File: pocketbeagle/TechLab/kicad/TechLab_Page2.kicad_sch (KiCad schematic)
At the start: 50 parts, among them J2 USB_C_Receptacle_USB2.0, J5 JST-SH-3P, T1 EAALSTIC1708A0, T2 3904, U5 MCP23S18-E/MJ, U6 FT230XQ-R, U7 SN74LV4053A

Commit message: TechLab: fix some reference designators
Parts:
- renumbered C11 to C10, C8 to C11, C9 to C8, R3 to R1, R7 to R10, R23 to R19, R4 to R2, R24 to R20, R10 to R21, R21 to R22, R6 to R3, R22 to R4, R9 to R6, R2 to R7, R1 to R9, T2 to T1, T1 to T2
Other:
- moved on the sheet: J5, R25, U7

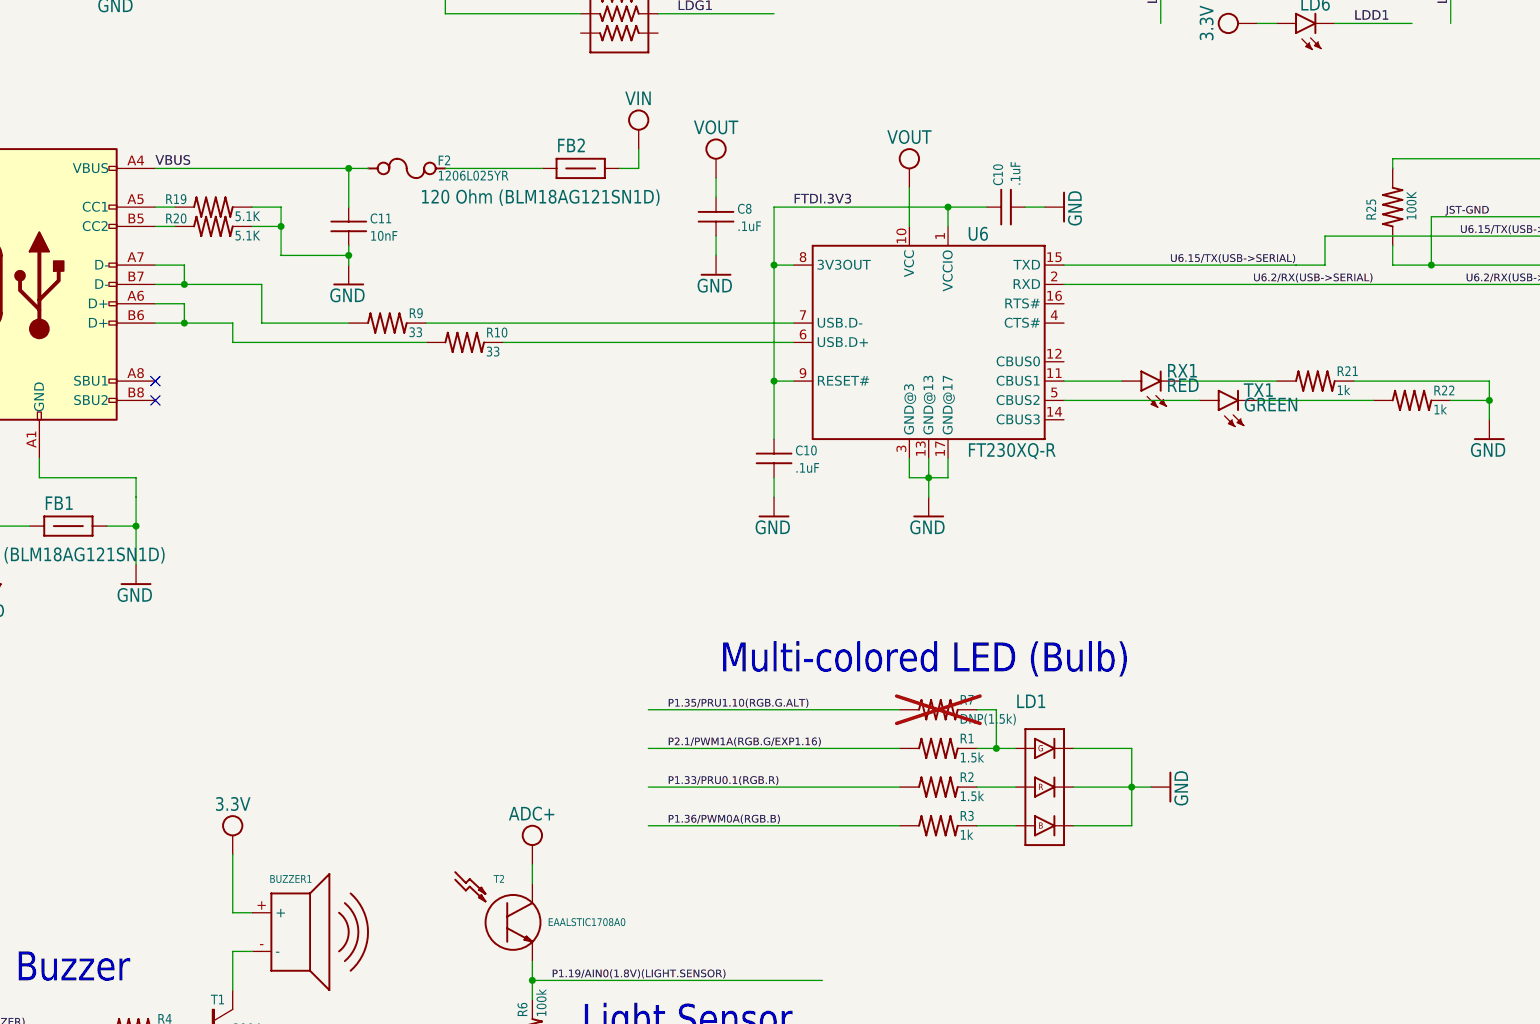
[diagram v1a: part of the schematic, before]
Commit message: TechLab: BOM and RefDes updates
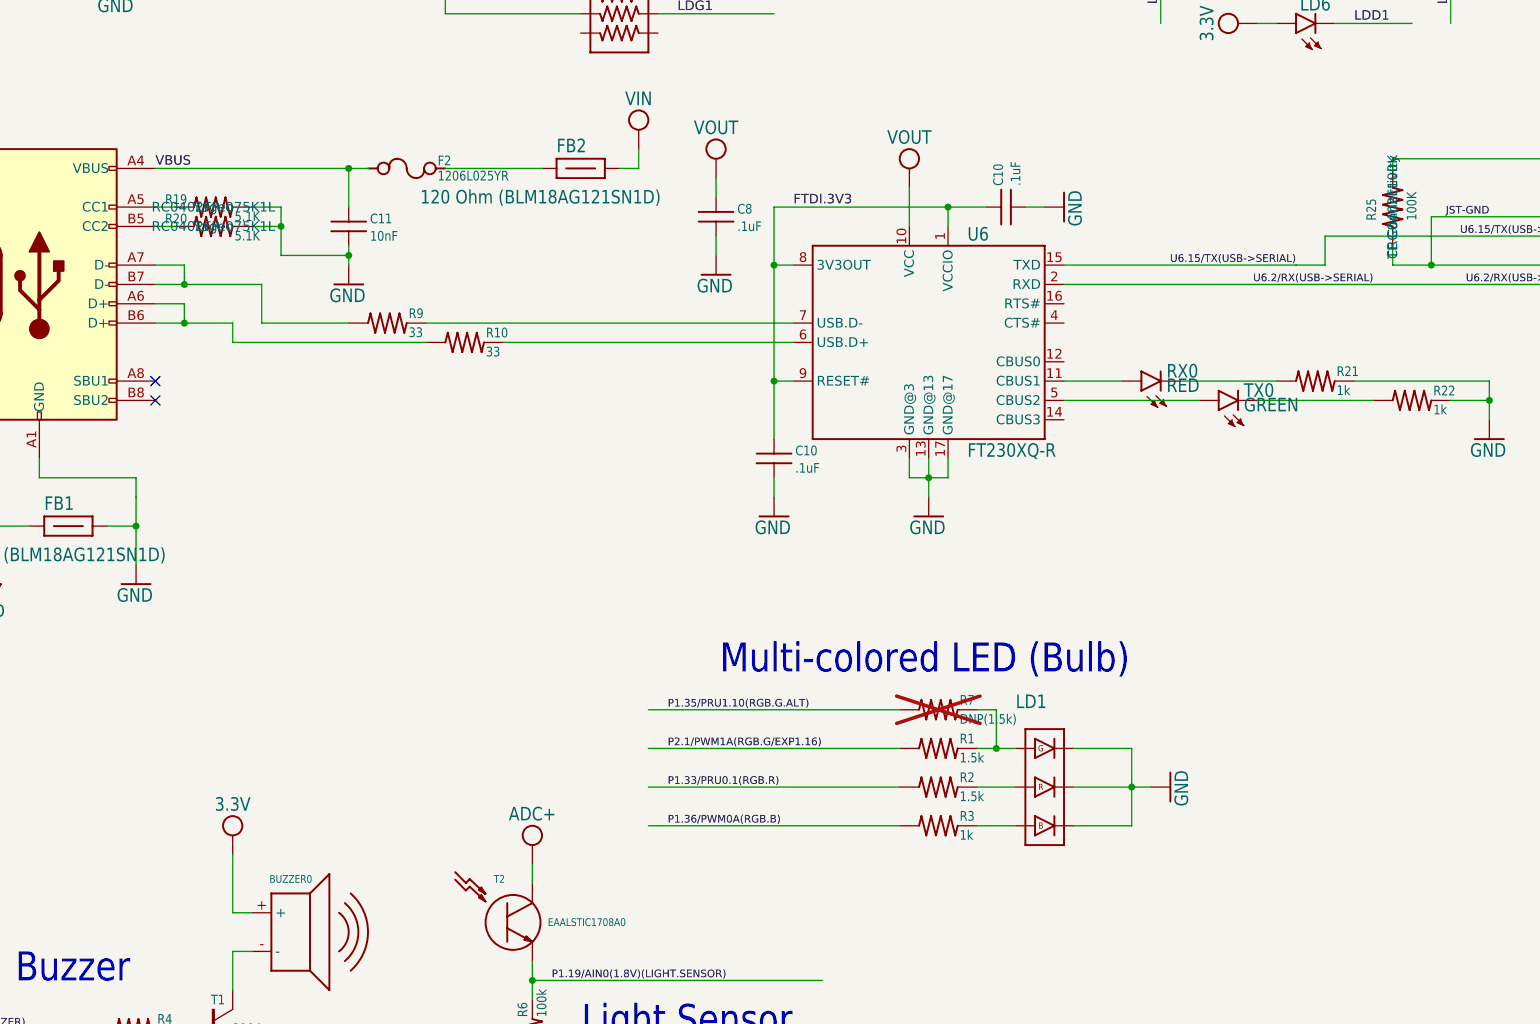
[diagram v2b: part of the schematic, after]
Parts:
- R19, R20: MANUFACTURER (none) -> Yageo; MPN (none) -> RC0402FR-075K1L
- R25: MANUFACTURER (none) -> TE Connectivity; MPN (none) -> CRG0402F100K
- renumbered BUZZER1 to BUZZER0, RX1 to RX0, TX1 to TX0
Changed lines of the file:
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@@
 		(on_board yes)
 		(dnp no)
-		(property "Reference" "RX1"
+		(property "Reference" "RX0"
 			(at 172.212 114.046 90)
 			(effects
@@
 			(project "TechLab"
 				(path "/199e843b-8c9a-4ca8-a6e6-fde18a374d00/4dffbcbf-91b6-4a9c-9fc6-f872a45552ad"
-					(reference "RX1")
+					(reference "RX0")
 					(unit 1)
 				)
@@
 			)
 		)
-		(property "MPN" ""
+		(property "MPN" "RC0402FR-075K1L"
+			(at 46.99 93.98 0)
+			(effects
+				(font
+					(size 1.27 1.27)
+				)
+			)
+		)
+		(property "MANUFACTURER" "Yageo"
 			(at 46.99 93.98 0)
 			(effects
@@
 		(on_board yes)
 		(dnp no)
-		(property "Reference" "BUZZER1"
+		(property "Reference" "BUZZER0"
 			(at 54.356 180.34 0)
 			(effects
@@
 			(project "TechLab"
 				(path "/199e843b-8c9a-4ca8-a6e6-fde18a374d00/4dffbcbf-91b6-4a9c-9fc6-f872a45552ad"
-					(reference "BUZZER1")
+					(reference "BUZZER0")
 					(unit 1)
 				)
@@
 			)
 		)
-		(property "MPN" ""
+		(property "MPN" "CRG0402F100K"
+			(at 201.93 91.44 0)
+			(effects
+				(font
+					(size 1.27 1.27)
+				)
+			)
+		)
+		(property "MANUFACTURER" "TE Connectivity"
 			(at 201.93 91.44 0)
 			(effects
@@
 		(on_board yes)
 		(dnp no)
-		(property "Reference" "TX1"
+		(property "Reference" "TX0"
 			(at 182.372 116.586 90)
 			(effects
@@
 			(project "TechLab"
 				(path "/199e843b-8c9a-4ca8-a6e6-fde18a374d00/4dffbcbf-91b6-4a9c-9fc6-f872a45552ad"
-					(reference "TX1")
+					(reference "TX0")
 					(unit 1)
 				)
@@
 			)
 		)
-		(property "MPN" ""
+		(property "MPN" "RC0402FR-075K1L"
+			(at 46.99 91.44 0)
+			(effects
+				(font
+					(size 1.27 1.27)
+				)
+			)
+		)
+		(property "MANUFACTURER" "Yageo"
 			(at 46.99 91.44 0)
 			(effects

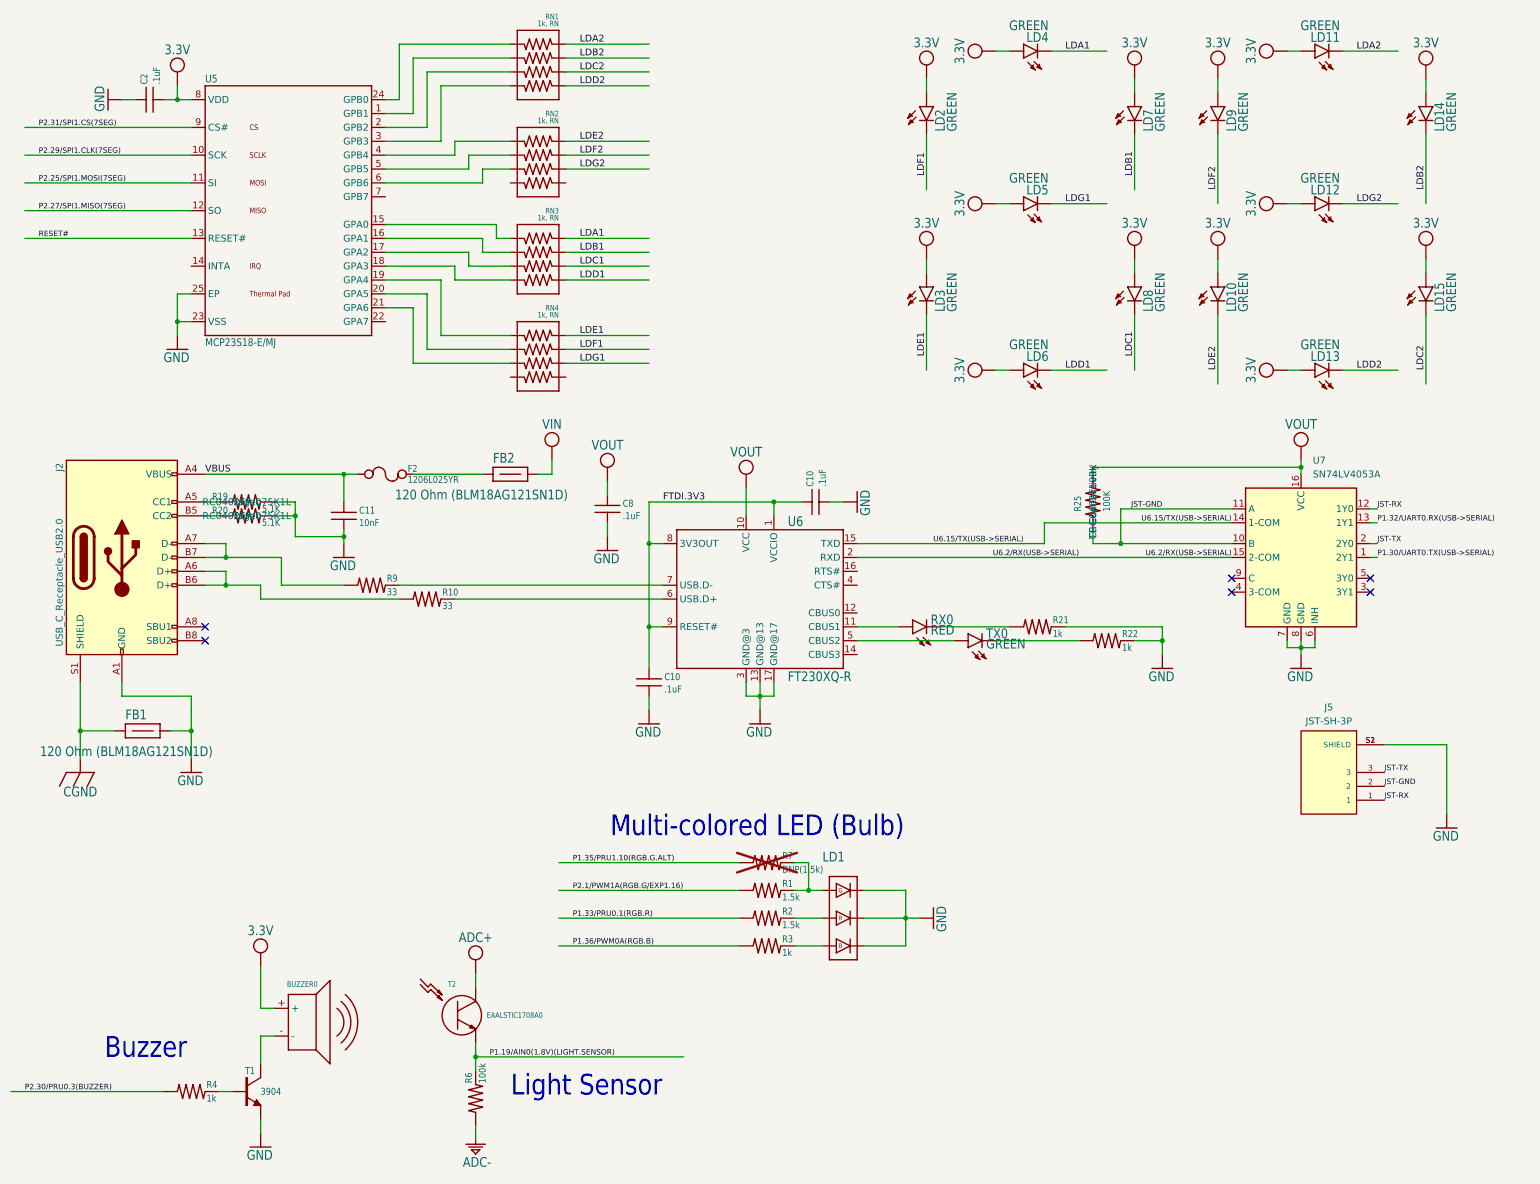
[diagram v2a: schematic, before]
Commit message: TechLab: RefDes and other cleanup, still needs forward annotation of PCB
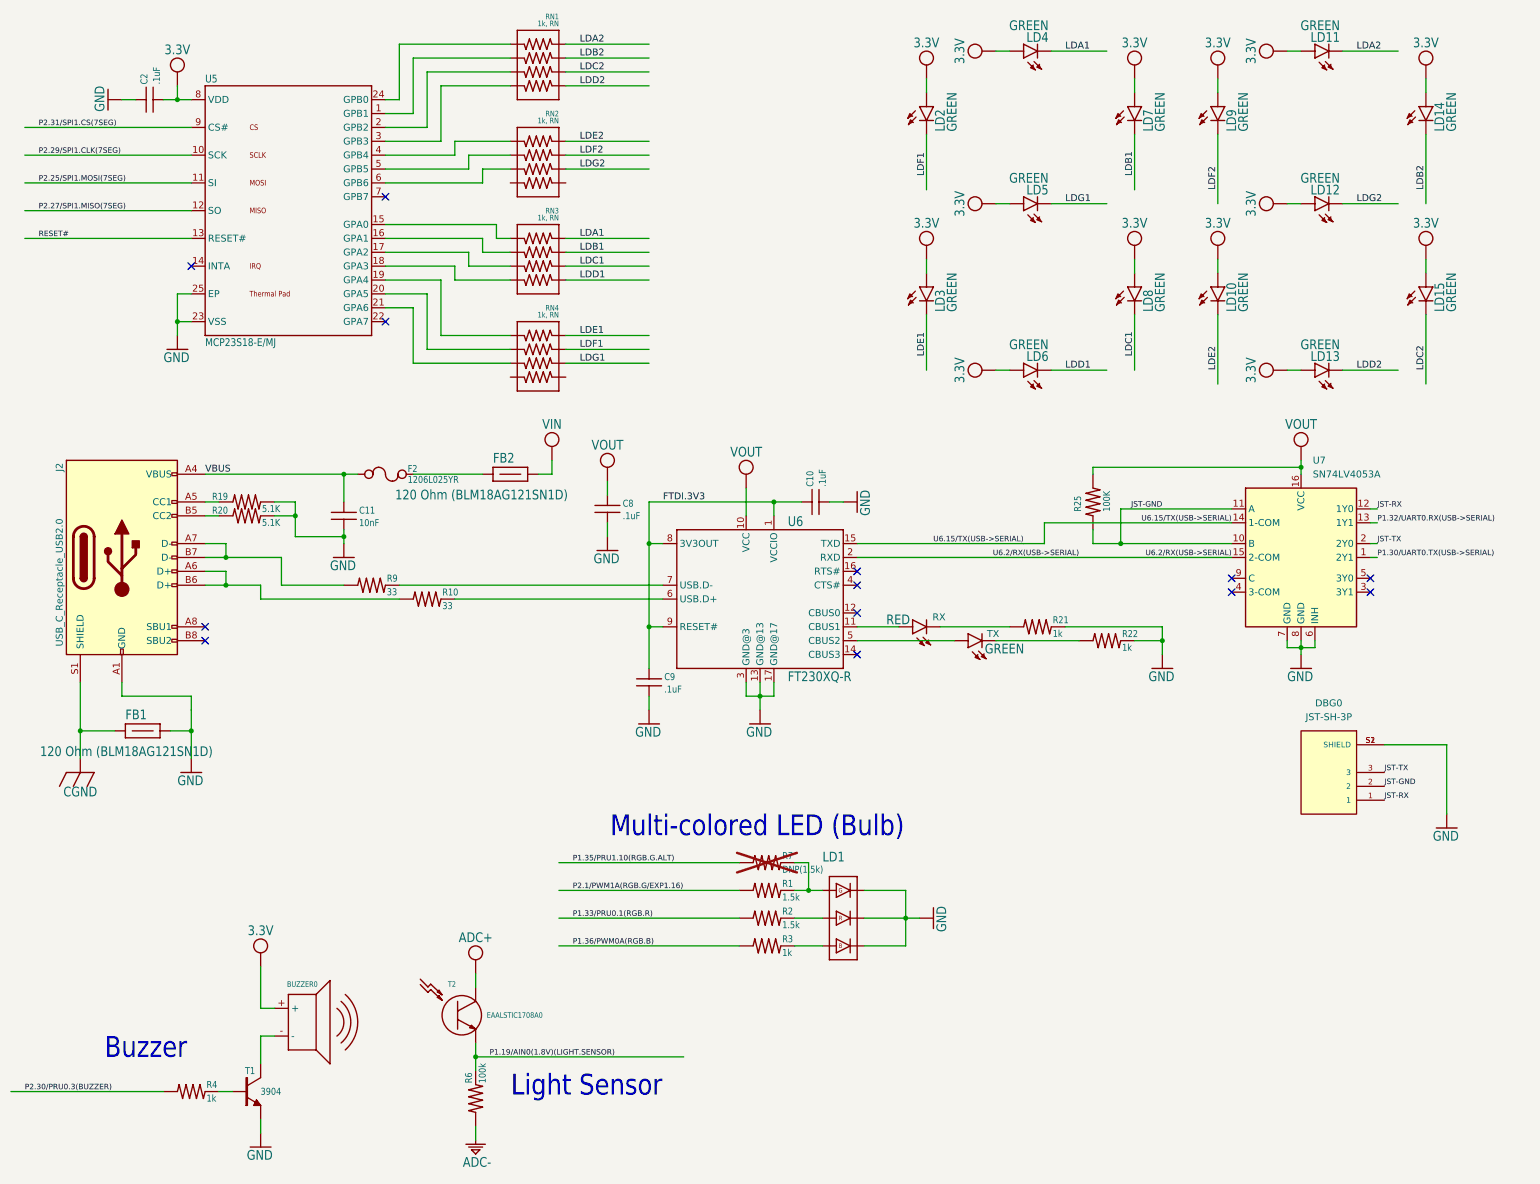
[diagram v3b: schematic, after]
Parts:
- renumbered C10 to C9, J5 to DBG0
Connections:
- no-connect marks 6 -> 13
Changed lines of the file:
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@@
 	)
 	(no_connect
+		(at 36.83 48.26)
+	)
+	(no_connect
+		(at 72.39 58.42)
+	)
+	(no_connect
 		(at 252.73 105.41)
 	)
@@
 	)
 	(no_connect
+		(at 72.39 35.56)
+	)
+	(no_connect
 		(at 39.37 116.84)
 	)
 	(no_connect
+		(at 158.75 106.68)
+	)
+	(no_connect
 		(at 252.73 107.95)
 	)
@@
 	)
 	(no_connect
+		(at 158.75 111.76)
+	)
+	(no_connect
 		(at 227.33 105.41)
 	)
+	(no_connect
+		(at 158.75 119.38)
+	)
+	(no_connect
+		(at 158.75 104.14)
+	)
 	(wire
 		(pts
@@
 				)
 				(justify right top)
+				(hide yes)
 			)
 		)
 		(property "Value" "RED"
-			(at 172.212 115.951 90)
+			(at 164.084 114.046 90)
 			(effects
 				(font
@@
 			)
 		)
-		(property "Description" ""
-			(at 168.91 114.3 0)
+		(property "Description" "RX"
+			(at 173.736 112.522 90)
 			(effects
 				(font
 					(size 1.27 1.27)
 				)
-				(hide yes)
 			)
 		)
@@
 		(on_board yes)
 		(dnp no)
-		(property "Reference" "C10"
+		(property "Reference" "C9"
 			(at 123.444 124.206 0)
 			(effects
@@
 			(project "TechLab"
 				(path "/199e843b-8c9a-4ca8-a6e6-fde18a374d00/4dffbcbf-91b6-4a9c-9fc6-f872a45552ad"
-					(reference "C10")
+					(reference "C9")
 					(unit 1)
 				)
@@
 					(size 1.27 1.27)
 				)
+				(hide yes)
 			)
 		)
@@
 					(size 1.27 1.27)
 				)
+				(hide yes)
 			)
 		)
@@
 					(size 1.27 1.27)
 				)
+				(hide yes)
 			)
 		)
@@
 					(size 1.27 1.27)
 				)
+				(hide yes)
 			)
 		)
@@
 				)
 				(justify right top)
+				(hide yes)
 			)
 		)
 		(property "Value" "GREEN"
-			(at 182.372 118.491 90)
+			(at 182.118 119.38 90)
 			(effects
 				(font
@@
 			)
 		)
-		(property "Description" ""
-			(at 179.07 116.84 0)
+		(property "Description" "TX"
+			(at 183.642 115.57 90)
 			(effects
 				(font
 					(size 1.27 1.27)
 				)
-				(hide yes)
 			)
 		)
@@
 					(size 1.27 1.27)
 				)
+				(hide yes)
 			)
 		)
@@
 					(size 1.27 1.27)
 				)
+				(hide yes)
 			)
 		)
@@
 		(dnp no)
 		(fields_autoplaced yes)
-		(property "Reference" "J5"
-			(at 245.11 129.032 0)
+		(property "Reference" "DBG0"
+			(at 245.11 128.27 0)
 			(effects
 				(font
@@
 		)
 		(property "Value" "JST-SH-3P"
-			(at 245.11 131.572 0)
+			(at 245.11 130.81 0)
 			(effects
 				(font
@@
 			(project "TechLab"
 				(path "/199e843b-8c9a-4ca8-a6e6-fde18a374d00/4dffbcbf-91b6-4a9c-9fc6-f872a45552ad"
-					(reference "J5")
+					(reference "DBG0")
 					(unit 1)
 				)
